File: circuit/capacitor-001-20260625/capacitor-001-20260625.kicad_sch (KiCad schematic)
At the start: 5 parts, among them J1 Conn_01x02_Pin

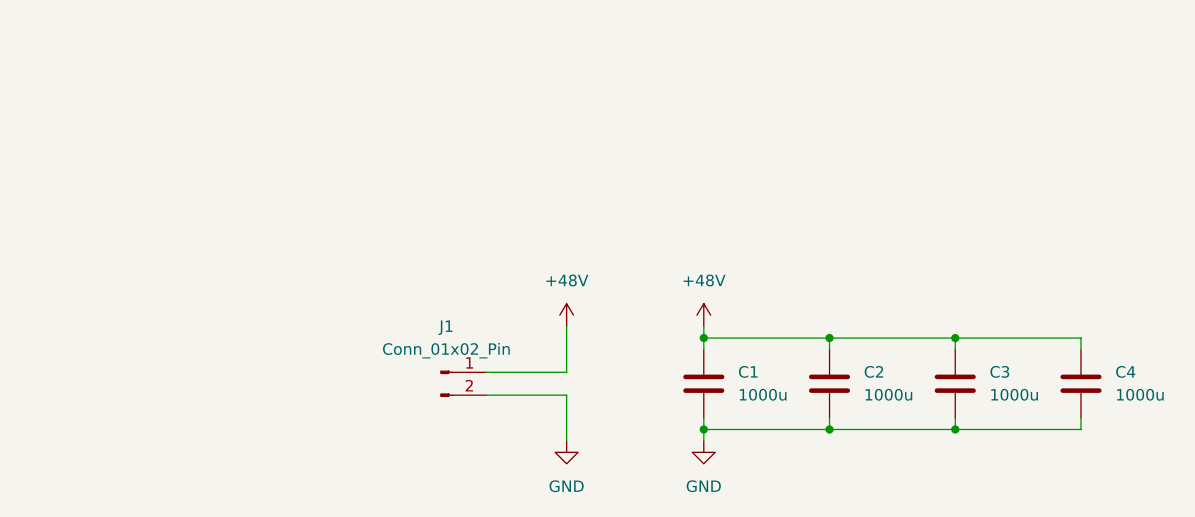
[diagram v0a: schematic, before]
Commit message: Update コンデンサ基板のボード図を完成させた
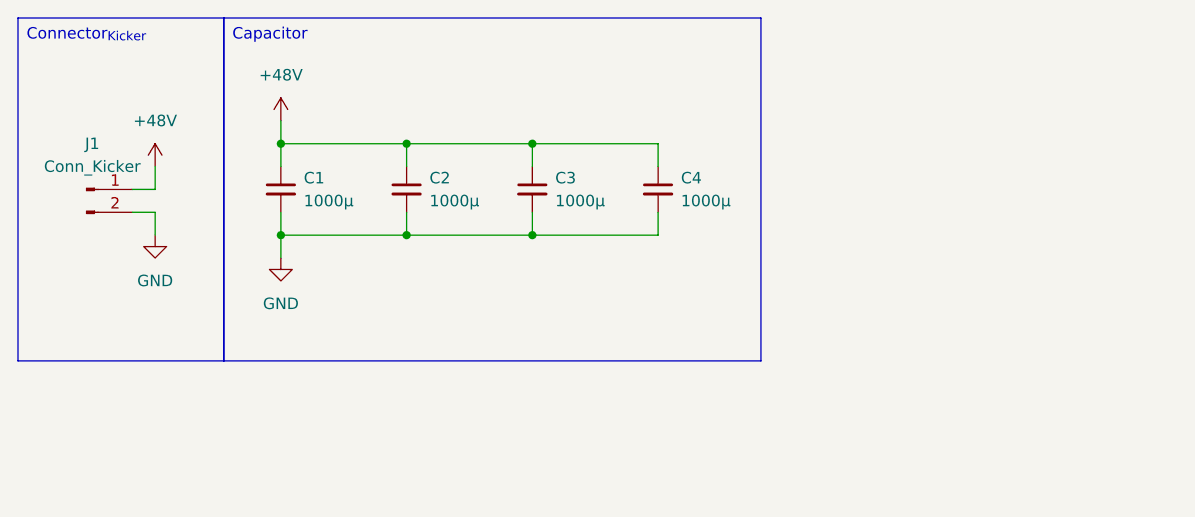
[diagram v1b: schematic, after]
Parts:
- removed C1, C2, C3, C4: 1000u, Capacitor_THT:CP_Radial_D12.5mm_P5.00mm, symbol Device:C
- added C1, C2, C3, C4: 1000μ, Capacitor_THT:CP_Radial_D12.5mm_P5.00mm, symbol Device:C_Small
- J1: value Conn_01x02_Pin -> Conn_Kicker
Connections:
- net +48V: now also C1.1, C2.1, C3.1, C4.1
- net GND: now also C1.2, C2.2, C3.2, C4.2
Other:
- moved on the sheet: J1
